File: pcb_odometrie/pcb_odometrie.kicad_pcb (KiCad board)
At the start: 4 copper layers, 43.5 x 57 mm, 42 parts, among them J1 USB_C_Receptacle_USB2.0_16P, J10 Conn_01x06, J11 Conn_01x06, J12 Conn_01x06, J13 Conn_01x06, J2 Conn_ST_STDC14, J3 1755736, J4 Conn_02x05_Row_Letter_First, J5 Conn_02x04_Row_Letter_First, J6 Conn_01x06, J7 Conn_01x06, J8 Conn_01x06, J9 Conn_01x06, U1 STM32G491KEU6, U2 MCP23017T-E/SO

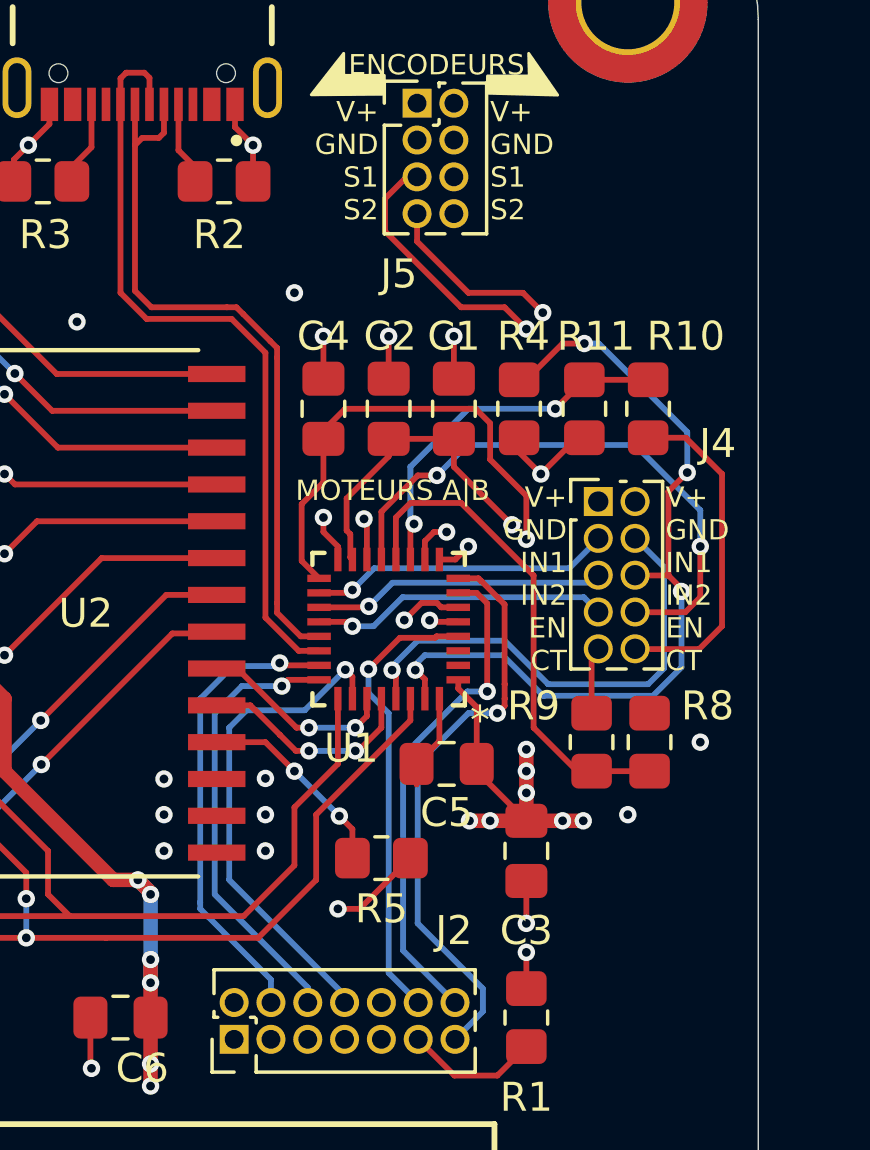
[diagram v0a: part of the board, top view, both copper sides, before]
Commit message: changement pin encodeur pour avoir la fonction timer
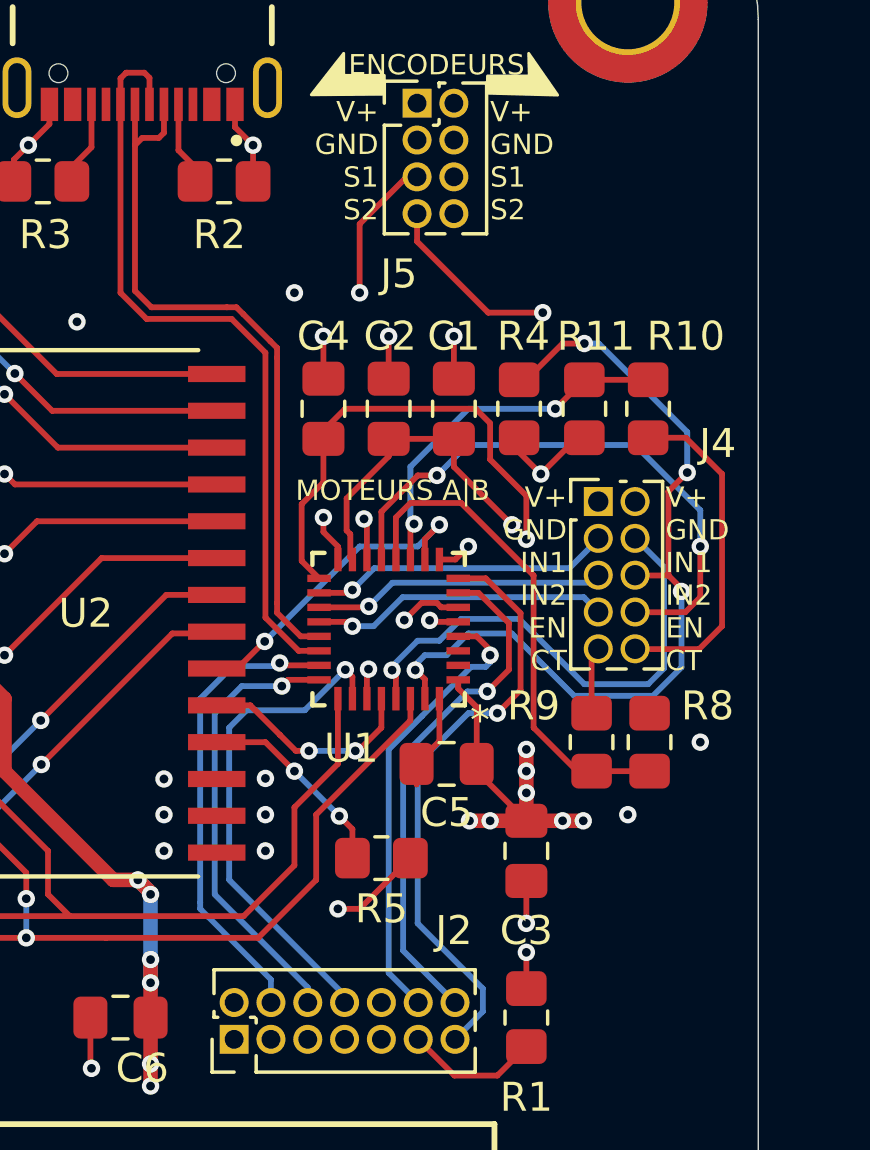
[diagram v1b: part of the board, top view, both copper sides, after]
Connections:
- U1 pad 10: Net-(J5-Pin_a3) -> /EVENTOUTA
- U1 pad 27: /EVENTOUTA -> Net-(J5-Pin_a3)
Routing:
- net /EVENTOUTA: track 6.79 -> 11.1 mm
- net Net-(J5-Pin_a3): track 18.5 -> 19.9 mm
- net Net-(J2-VCP_TX): track 17.3 -> 17.9 mm
- net /IN2B: track 28.9 -> 29.5 mm
- net /IN1B: track 16.6 -> 17.3 mm
- net Net-(J2-VCP_RX): track 20.1 -> 20.7 mm

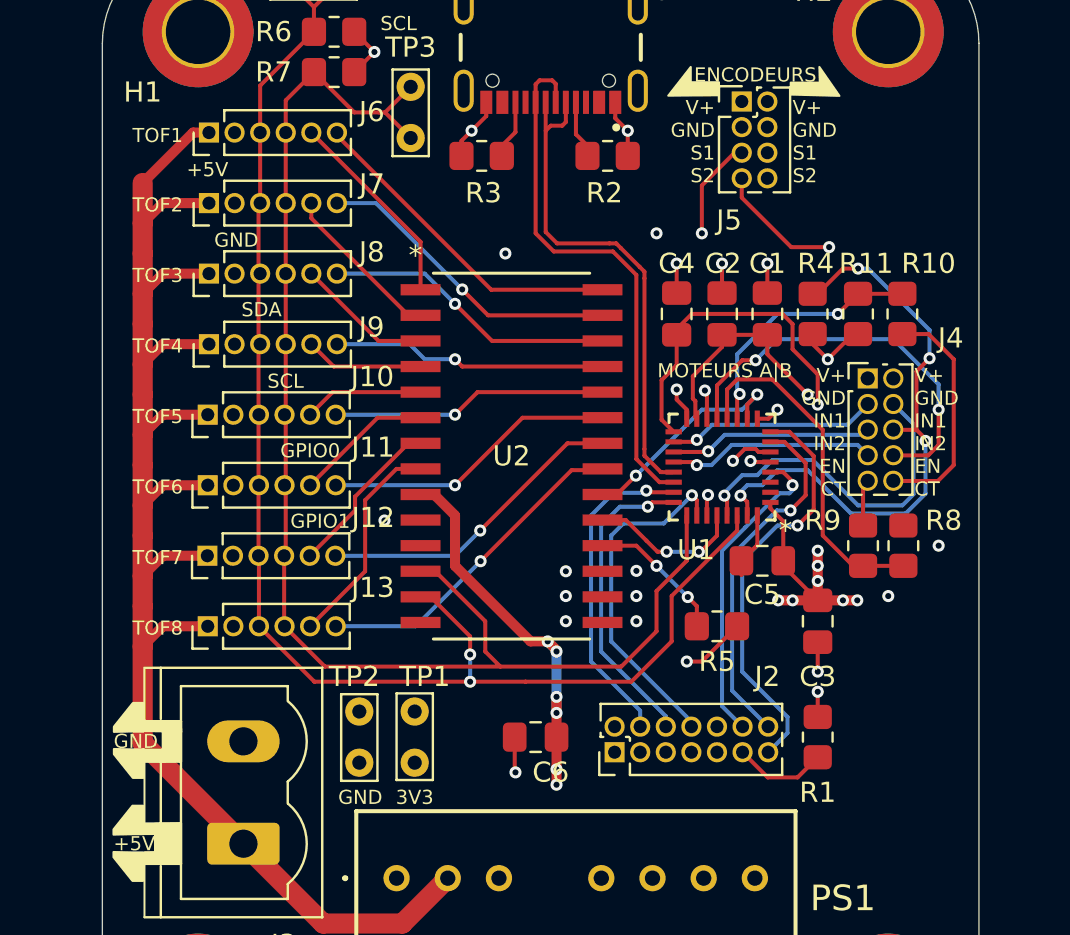
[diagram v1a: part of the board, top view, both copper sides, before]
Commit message: connecteur 14pin avec detrompage + renumerotation TOF
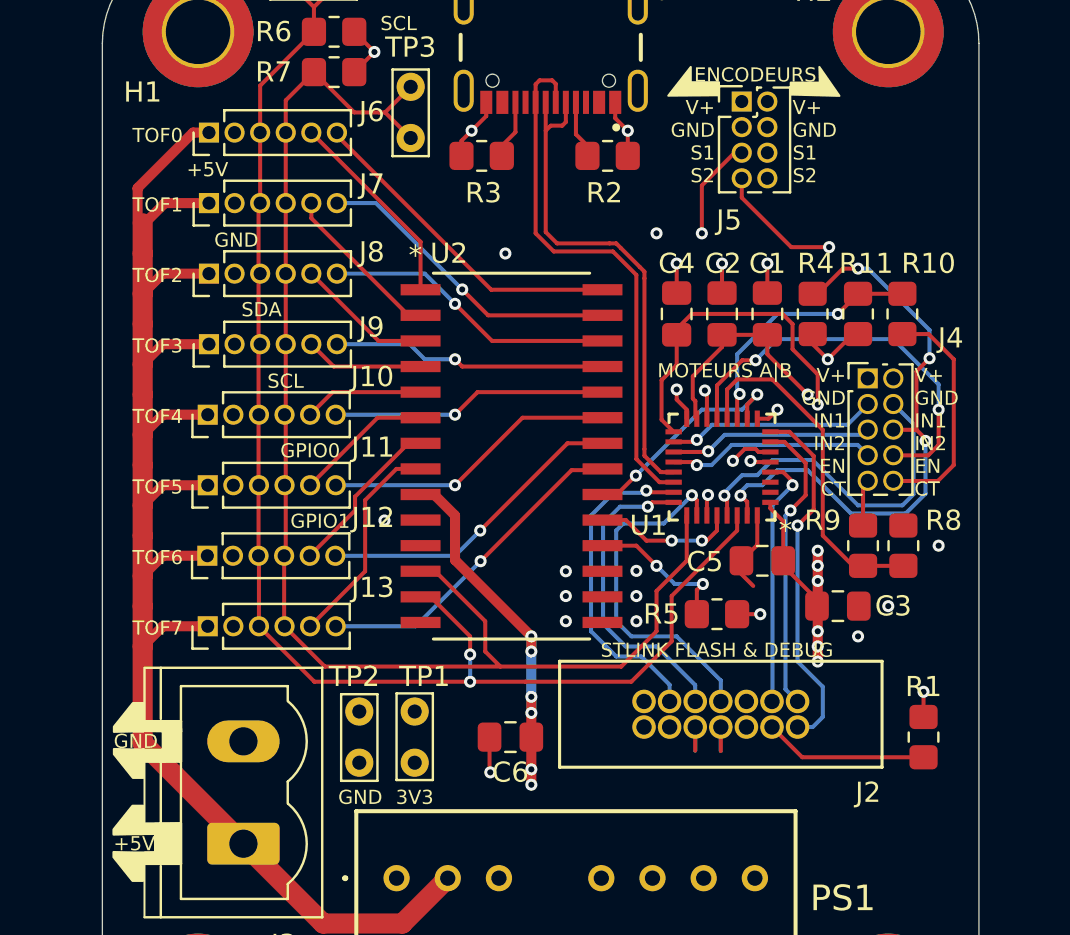
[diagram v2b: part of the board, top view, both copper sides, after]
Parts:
- J2: footprint Connector_PinHeader_1.27mm:PinHeader_2x07_P1.27mm_Vertical -> Modelec:CONN14_3220-14_CNC
- R10, R8: value 402 -> 402R
- moved R1 5.25 mm to (211.2, 82.0)
- moved J2 2.91 mm to (197.4, 80.2), turned to 0 degrees
- moved C3 1.25 mm to (207.0, 75.5), turned to 0 degrees
- moved C6 1.25 mm to (190.8, 82.0)
- moved R5 0.60 mm to (201.0, 75.9)
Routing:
- net GND: track 25.2 -> 31.6 mm
- net Net-(J2-GNDDetect): track 4.66 -> 8.14 mm
- net Net-(J2-VCP_TX): track 17.9 -> 14.7 mm
- net Net-(J2-~{RST}): track 15.6 -> 12.6 mm
- net Net-(J2-VCP_RX): track 20.7 -> 17.9 mm
- net +3V3: track 74.6 -> 71.8 mm, vias 17 -> 16
- net /EVENTOUTB: track 7.66 -> 7.06 mm
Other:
- board text added: "STLINK FLASH & DEBUG"
- board text added: "TOF0"
- board text removed: "TOF8"

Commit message: version finale PCB odometrie
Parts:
- J4: value Conn_02x05_Row_Letter_First -> Conn_02x06_Row_Letter_First; footprint Connector_PinSocket_1.27mm:PinSocket_2x05_P1.27mm_Vertical -> Connector_PinSocket_2.54mm:PinSocket_2x06_P2.54mm_Vertical
- R10, R8: value 402R -> 402
- moved R8 7.20 mm to (210.8, 79.2)
- moved R9 7.20 mm to (212.8, 79.2)
- moved H3 4.92 mm to (214.0, 96.5)
- moved H2 4.74 mm to (214.0, 45.5)
- moved R1 4.59 mm to (208.4, 85.6), turned to 0 degrees
- moved R10 3.22 mm to (212.5, 58.8)
- moved R11 3.22 mm to (210.3, 58.8)
- moved H4 2.66 mm to (173.5, 96.5)
- moved H1 2.30 mm to (173.5, 45.5)
- moved J4 2.04 mm to (211.5, 62.8)
- moved C3 0.75 mm to (206.2, 75.5), turned to 180 degrees
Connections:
- J4 pad a2: /IN1A -> GND
- J4 pad a3: /IN2A -> /IN1A
- J4 pad a4: /ENA -> /IN2A
- J4 pad a5: /CTA -> /ENA
- J4 pad b2: /IN1B -> GND
- J4 pad b3: /IN2B -> /IN1B
- J4 pad b4: /ENB -> /IN2B
- J4 pad b5: /CTB -> /ENB
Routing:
- net /ADC2_IN4: track 17.3 -> 24.8 mm
- net GND: track 31.6 -> 25.6 mm, vias 22 -> 110
- net /CTB: track 11.6 -> 17.1 mm
- net /ENA: track 10.3 -> 15.3 mm, vias 1 -> 2
- net /IN2A: track 10.1 -> 13.4 mm, vias 1 -> 2
- net /IN2B: track 29.5 -> 32.6 mm, vias 4 -> 2
- net /IN1B: track 17.3 -> 14.5 mm
- net Net-(J2-GNDDetect): track 8.14 -> 6.09 mm
- net /IN1A: track 10.4 -> 12.4 mm
- net /ADC2_IN3: track 12.7 -> 14.6 mm
- net /ENB: track 20.5 -> 19.5 mm
- net /CTA: track 2.31 -> 2.97 mm
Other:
- board size 43.5 x 57 mm -> 46.5 x 57 mm
- board text removed: "MOTEURS A|B"
- board text removed: "V+ GND IN1 IN2 EN CT"

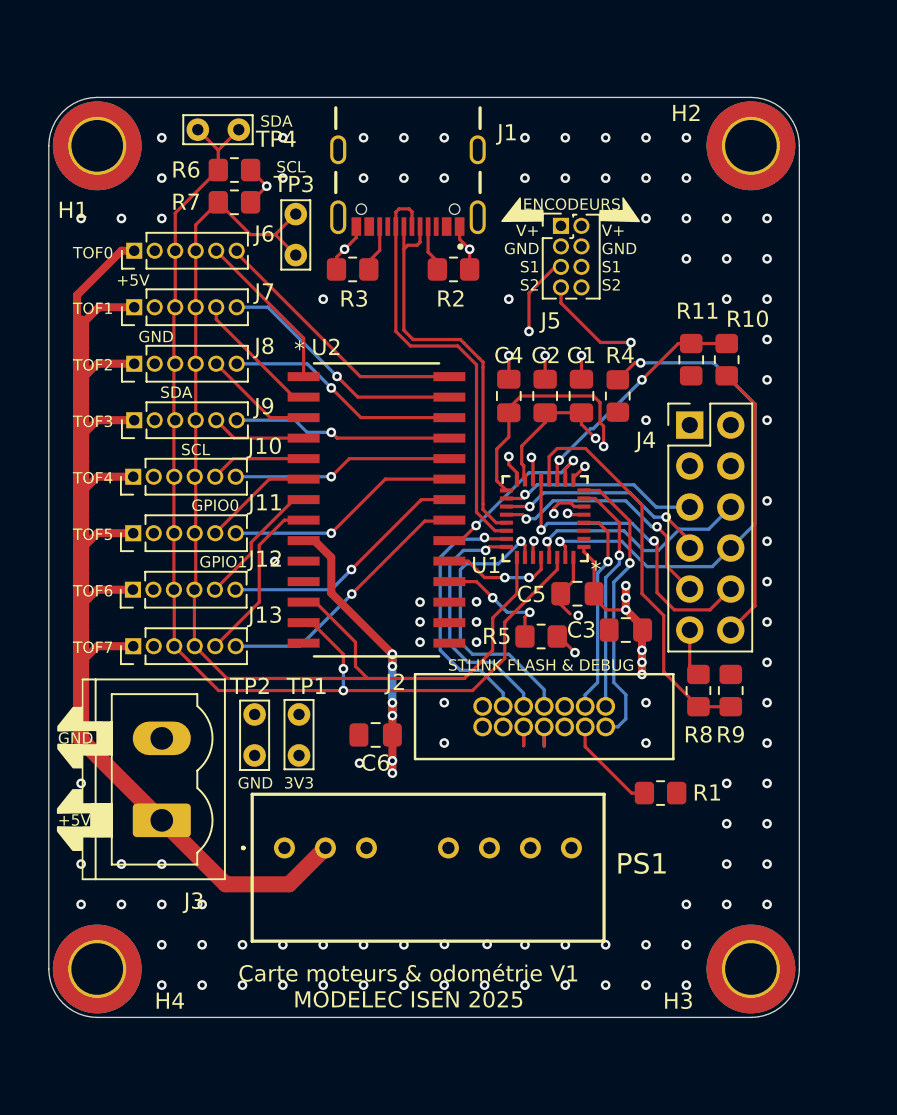
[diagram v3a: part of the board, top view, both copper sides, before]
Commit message: ajustement pos pins pcb odometrie + 3 batteries et TODOs sur le schema pcb pamis
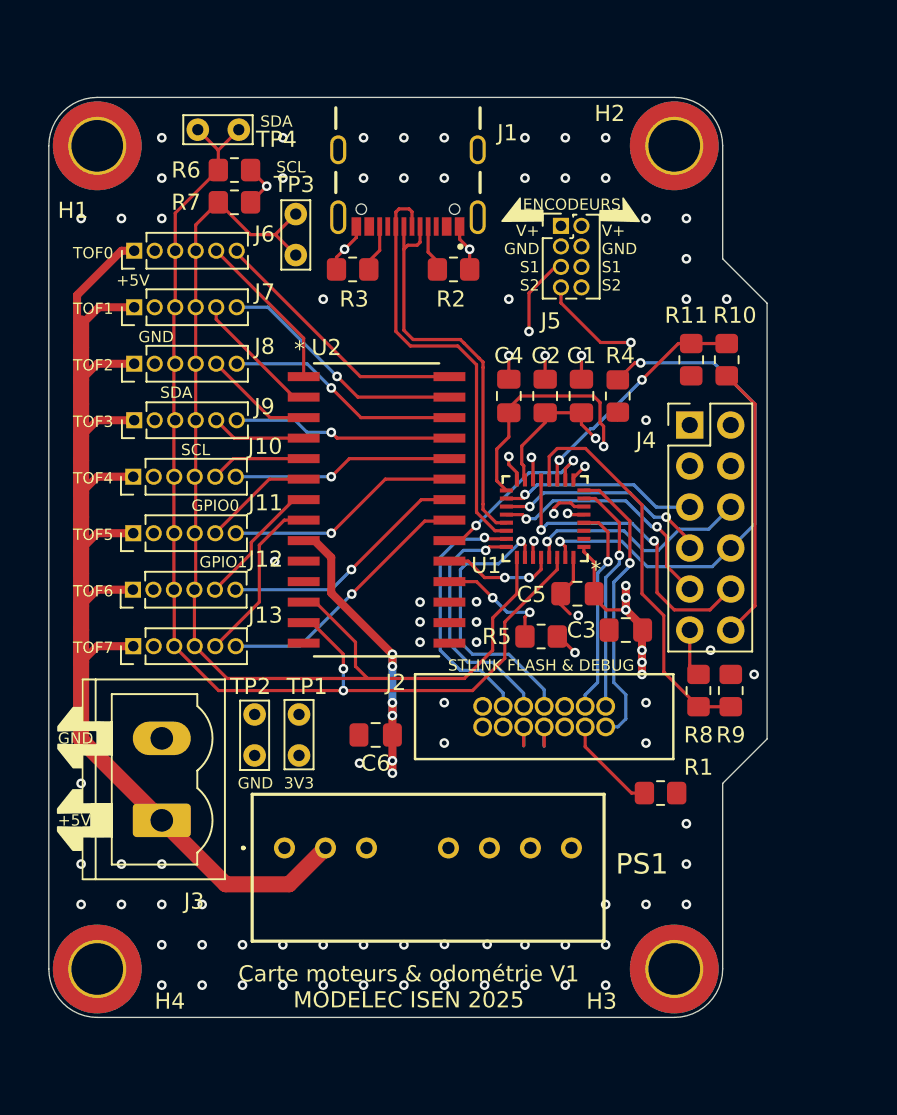
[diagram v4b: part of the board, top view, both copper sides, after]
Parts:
- moved H2 4.75 mm to (209.2, 45.5)
- moved H3 4.75 mm to (209.2, 96.5)
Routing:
- net GND: vias 110 -> 86
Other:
- board size 46.5 x 57 mm -> 44.5 x 57 mm

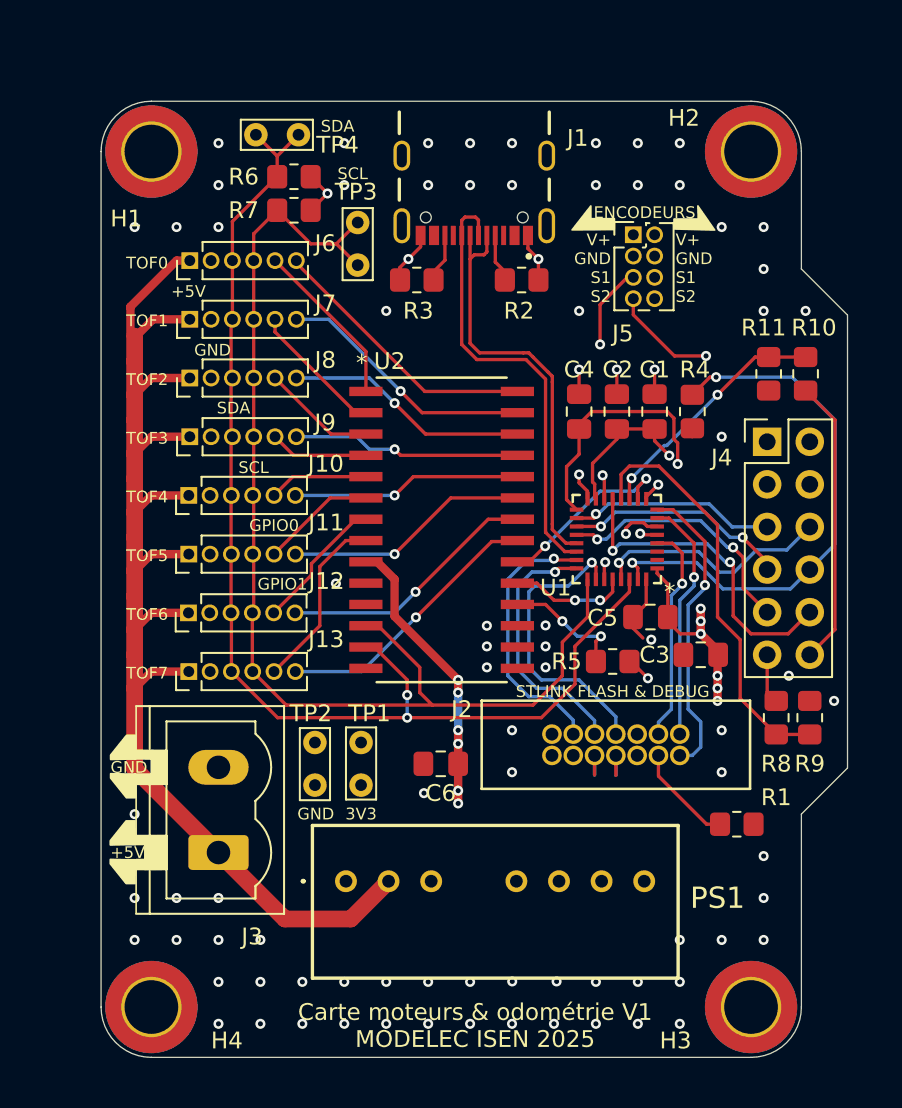
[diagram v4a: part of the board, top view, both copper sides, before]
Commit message: Ajout connecteurs, diodes sur arrêt moteurs et finalisation du schéma
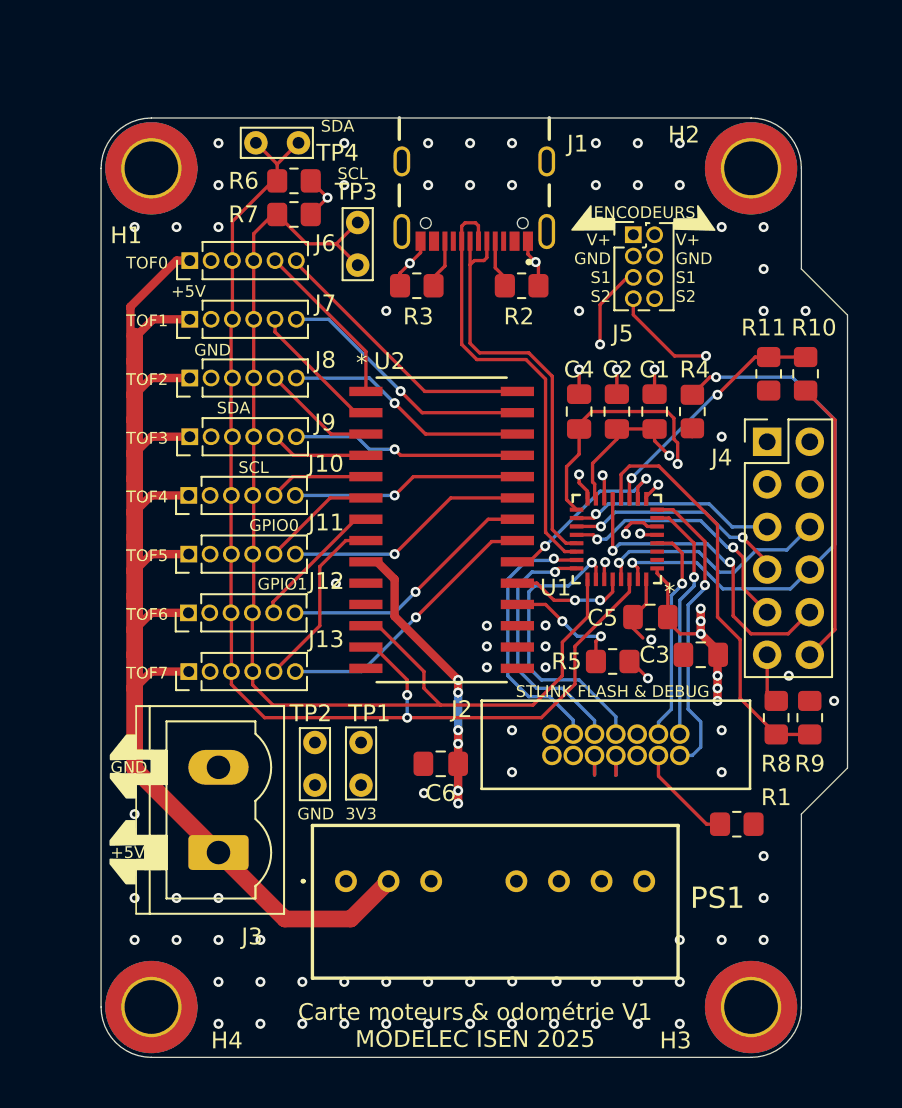
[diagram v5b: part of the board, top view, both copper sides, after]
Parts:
- added G***: LOGO, LOGO, B.Cu at (189.5, 71.0)
- moved G*** 5.13 mm to (191.5, 56.2)
- moved H1 1.00 mm to (173.5, 46.5)
- moved H2 1.00 mm to (209.2, 46.5)
- moved TP4 0.48 mm to (179.7, 45.0)
- moved J1 0.34 mm to (192.8, 46.1)
- moved R2 0.34 mm to (195.6, 53.5)
- moved R3 0.34 mm to (189.3, 53.5)
- moved R6 0.25 mm to (182.0, 49.2)
- moved R7 0.25 mm to (182.0, 47.2)
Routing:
- net Net-(J1-CC2): track 2.94 -> 2.44 mm
- net Net-(J1-CC1): track 2.89 -> 2.39 mm
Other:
- board size 44.5 x 57 mm -> 44.5 x 56 mm
- board text added: "PIT STOP"
